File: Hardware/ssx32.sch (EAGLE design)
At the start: 81 parts, among them IC1 PIC18F45K20, IC2 FT232RL, IC3 TXB0108PW, IC4 TXB0108PW, IC5 TXB0108PW, IC6 TXB0108PW, IC7 78L33, IC8 74AHC1G32DBV, X1 8, X10 1, X11 19, X12 16, X13 15, X14 14, X15 13, X16 12, X17 11, X18 10, X19 9, X20 20, X21 21, X22 22, X23 23, X24 24, X25 25, X26 26, X27 27, X28 28, X29 29, X3 17, X30 30, X31 31, X32 32, X33 1751248, X34 18, X35 USB, X4 7, X5 6, X6 5, X7 4, X8 3, X9 2

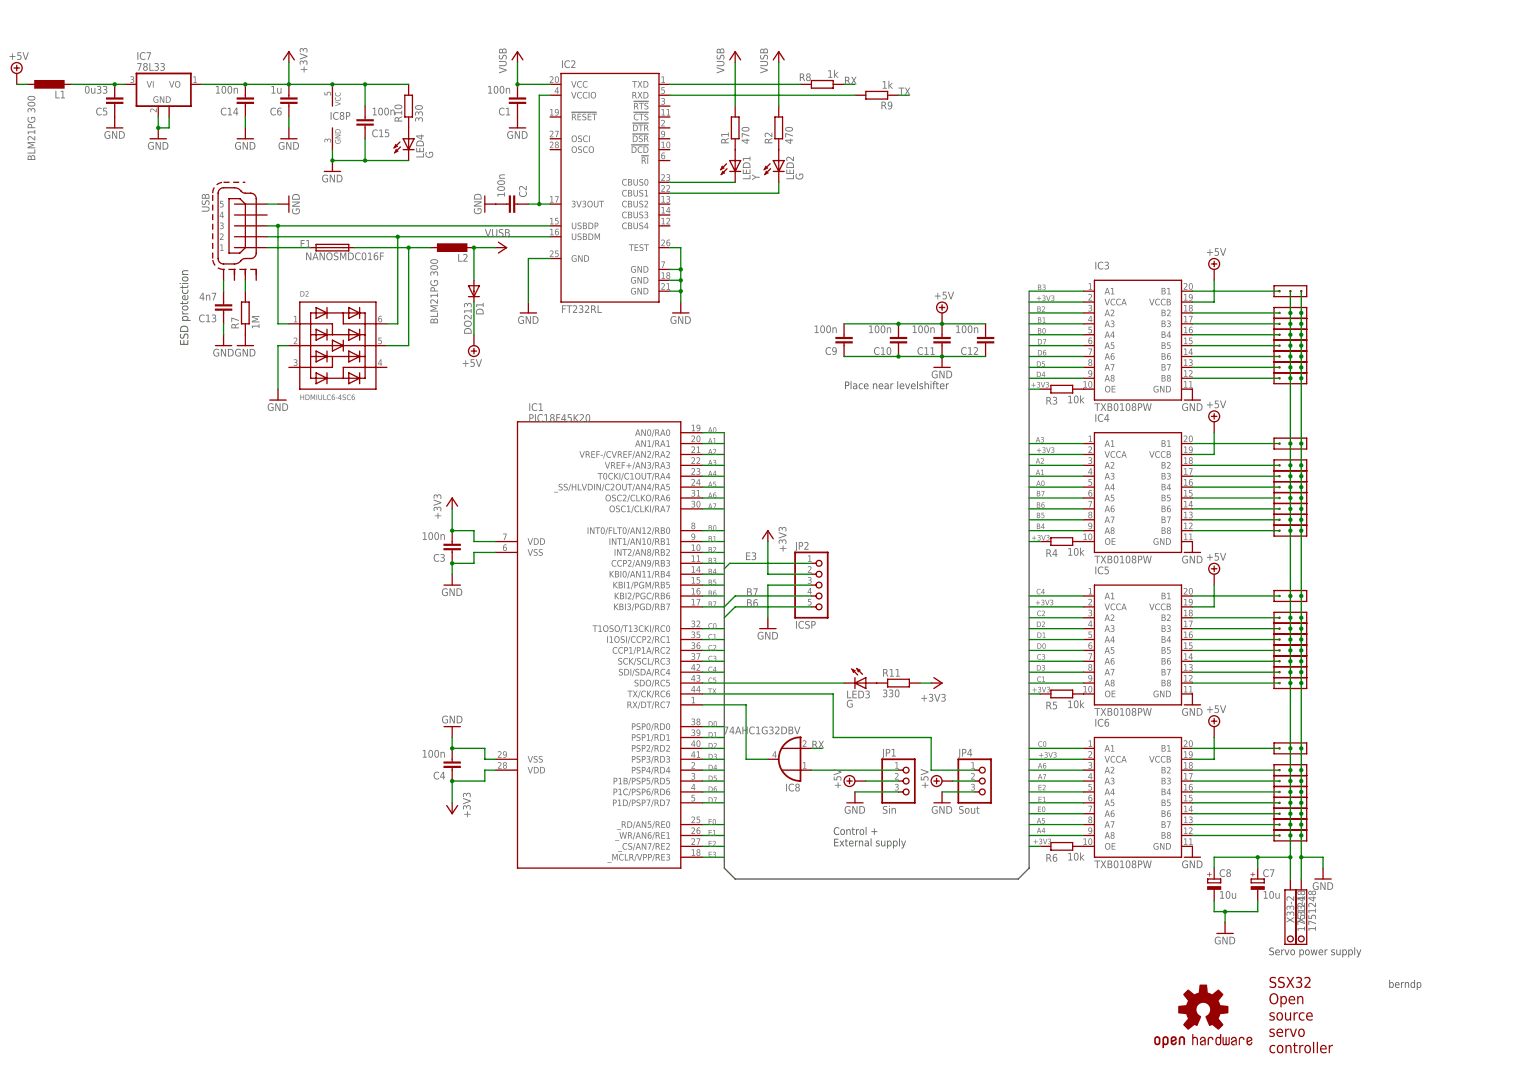
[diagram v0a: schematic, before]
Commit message: Fixed issues
Replaced OR with AND gate with pullups
Removed unnecessary ferrite bead
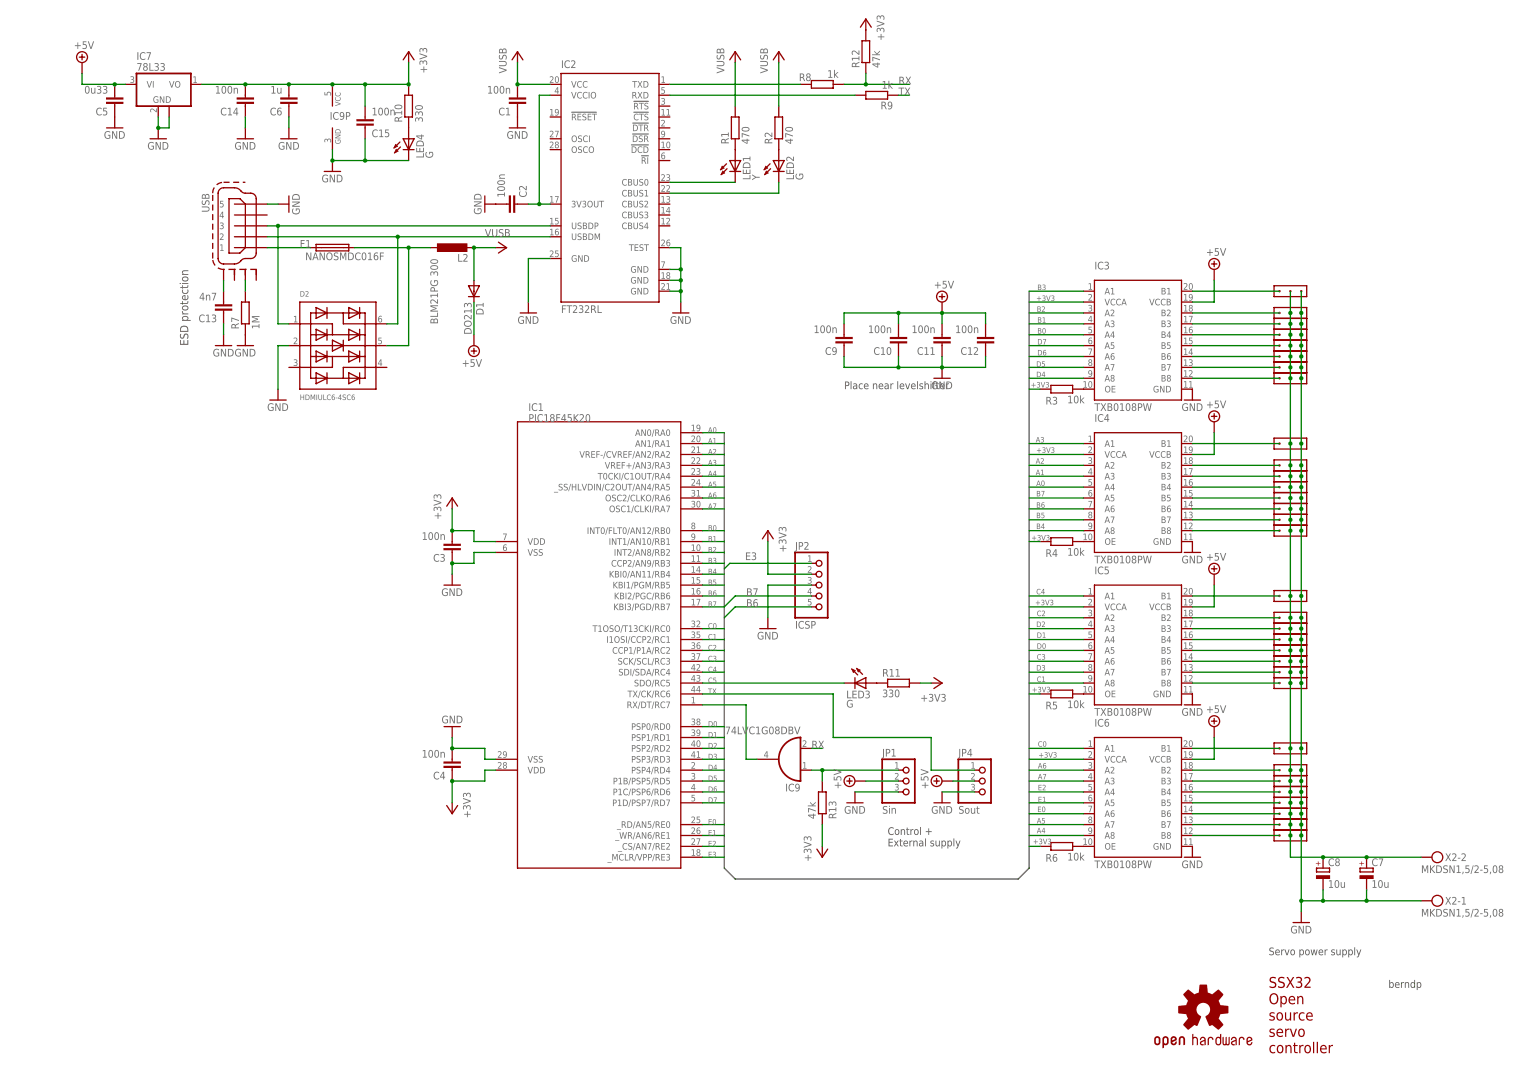
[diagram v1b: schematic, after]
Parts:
- removed IC8: 74AHC1G32DBV, 74xx-little-de:74AHC1G32DBV
- removed L1: BLM21PG 300, rcl:L-EU0805
- removed X33: 1751248, con-phoenix-350:1751248
- added IC9: 74LVC1G08DBV, 74xx-little-de:74LVC1G08DBV
- added R12, R13: 47k, rcl:R-EU_R0603
- added X2: MKDSN1,5/2-5,08, con-phoenix-508:MKDSN1,5/2-5,08
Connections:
- removed net N$46: C5.2, IC7.VI, L1.2
- net +3V3: now also IC9P.VCC, R12.2, R13.1; no longer IC8P.VCC
- net +UB: now also C5.2, IC7.VI; no longer L1.1
- net GND: now also IC9P.GND, X2-1.KL; no longer IC8P.GND, X33-1.K
- net N$48: now also IC9A.O; no longer IC8A.O
- net N$54: now also IC9A.I0, R13.2; no longer IC8A.I0
- net RX: now also IC9A.I1, R12.1; no longer IC8A.I1
- net VSERVO: now also X2-2.KL; no longer X33-2.K
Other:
- moved on the sheet: C7, C8
